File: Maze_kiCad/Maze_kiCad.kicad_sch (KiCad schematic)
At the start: 10 parts, among them J1 Screw_Terminal, U1 ESP32-S3-DevKitC-1, U10 L7805, U2 TCRT5000, U3 TCRT5000, U4 TCRT5000, U5 TCRT5000, U6 TCRT5000, U7 TCRT5000

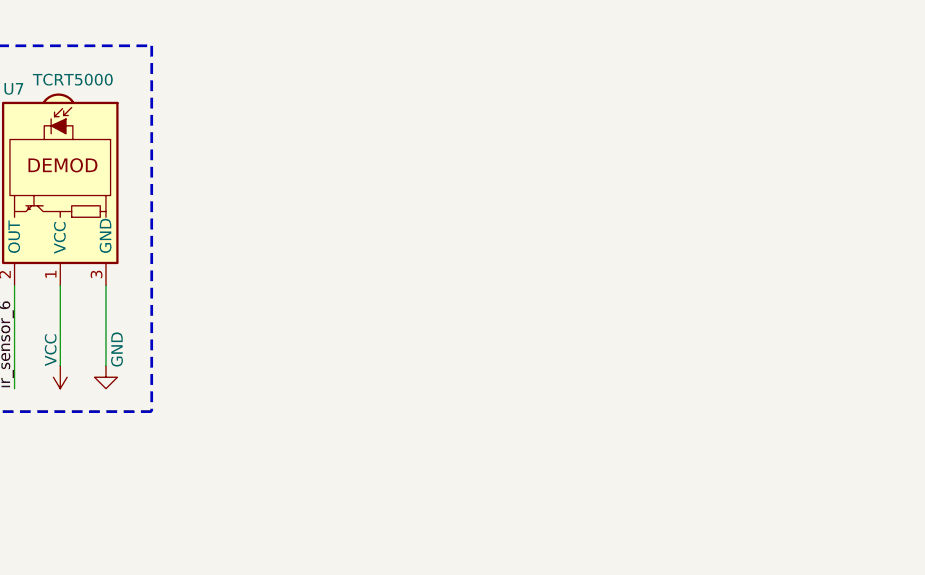
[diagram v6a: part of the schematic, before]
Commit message: Make all connections for drv8835, esp32-s3 and motors inputs
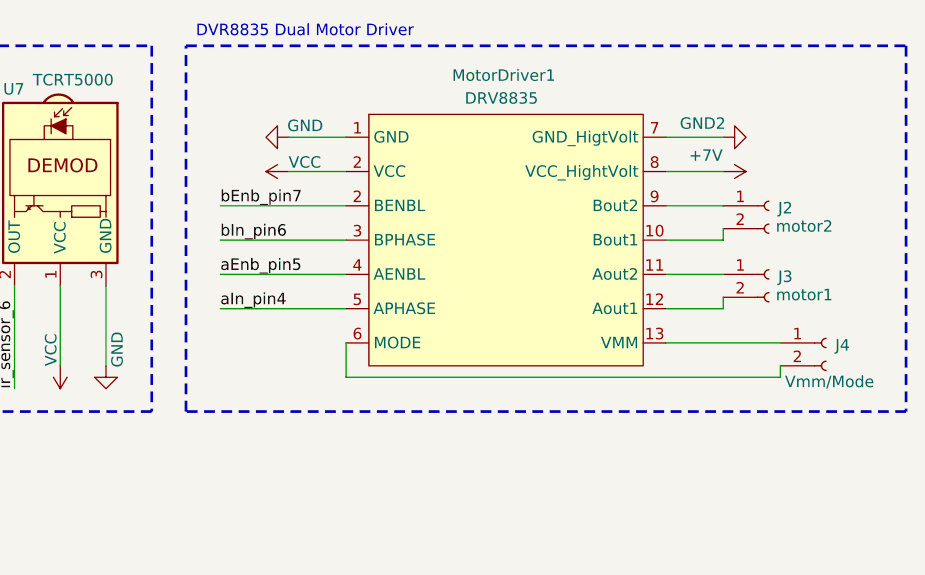
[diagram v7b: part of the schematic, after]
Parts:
- added J2: motor2, Connector_PinSocket_2.54mm:PinSocket_1x02_P2.54mm_Vertical, symbol Connector:Conn_01x02_Socket
- added J3: motor1, Connector_PinSocket_2.54mm:PinSocket_1x02_P2.54mm_Vertical, symbol Connector:Conn_01x02_Socket
- added J4: Vmm/Mode, Connector_PinSocket_2.54mm:PinSocket_1x02_P2.54mm_Vertical, symbol Connector:Conn_01x02_Socket
- added MotorDriver1: DRV8835, drv8835:drv8835, symbol drv8835:DRV8835
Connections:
- net +7V: now also MotorDriver1.8 (VCC_HightVolt)
- net GND: now also MotorDriver1.1 (GND)
- net GND2: now also MotorDriver1.7 (GND_HigtVolt)
- net VCC: now also MotorDriver1.2 (VCC)
- net aEnb_pin5: now also MotorDriver1.4 (AENBL)
- net aIn_pin4: now also MotorDriver1.5 (APHASE)
- net bEnb_pin7: now also MotorDriver1.2 (VCC)
- net bIn_pin6: now also MotorDriver1.3 (BPHASE)
- new net: J4.1 (Pin_1), MotorDriver1.13 (VMM)
- new net: J4.2 (Pin_2), MotorDriver1.6 (MODE)
- new net: J2.1 (Pin_1), MotorDriver1.9 (Bout2)
- new net: J2.2 (Pin_2), MotorDriver1.10 (Bout1)
- new net: J3.1 (Pin_1), MotorDriver1.11 (Aout2)
- new net: J3.2 (Pin_2), MotorDriver1.12 (Aout1)
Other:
- note added: "DVR8835 Dual Motor Driver"

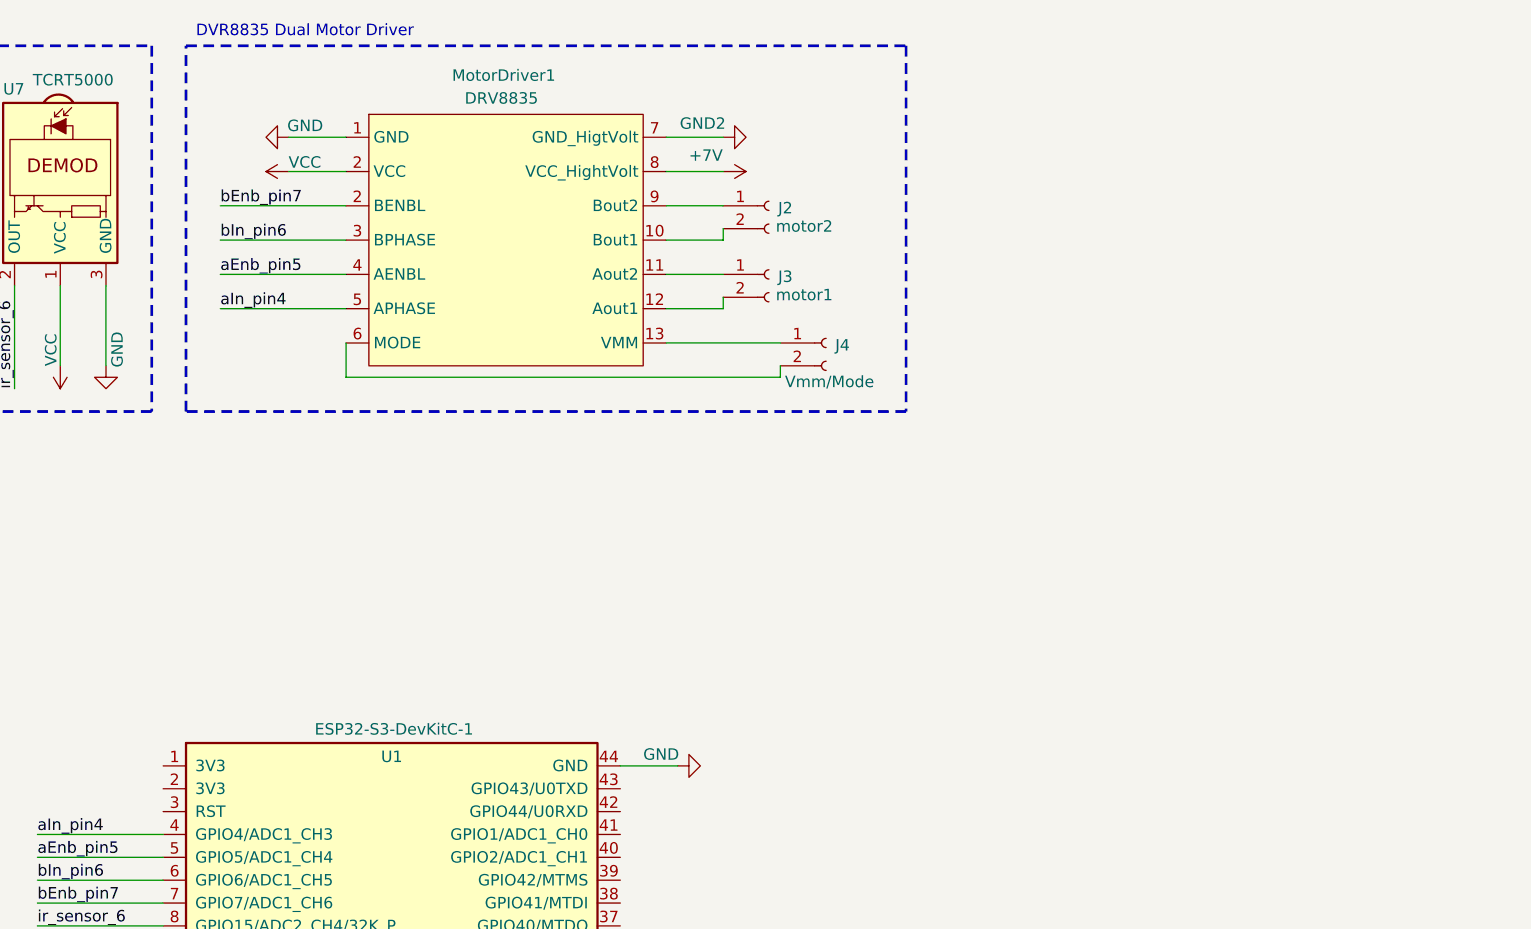
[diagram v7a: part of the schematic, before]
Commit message: Create connections for gyroscope and ultrasonic sensor with esp32-s3
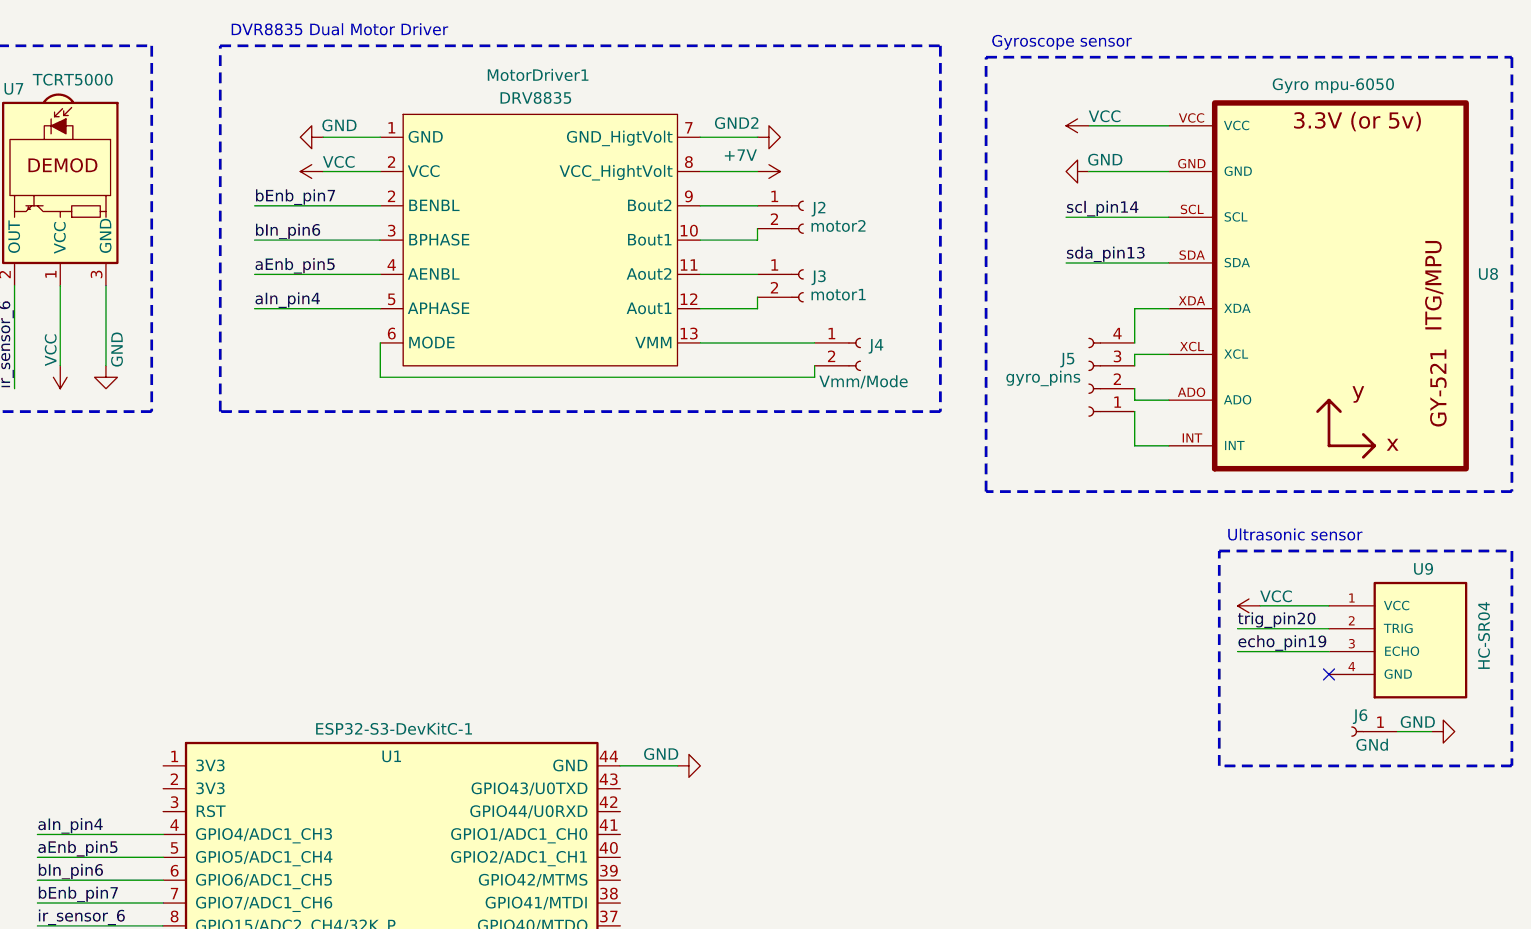
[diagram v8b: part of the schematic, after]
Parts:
- added J5: gyro_pins, symbol Connector:Conn_01x04_Socket
- added J6: GNd, symbol Connector:Conn_01x01_Socket
- added U8: Gyro mpu-6050, mpu6050:GY-521, symbol mpu6050:GY-521
- added U9: HC-SR04, ultrasonic:XCVR_HC-SR04, symbol ultrasonic:HC-SR04
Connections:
- net GND: now also J6.1 (Pin_1), U8.GND
- net VCC: now also U8.VCC, U9.1 (VCC)
- net echo_pin19: now also U9.3 (ECHO)
- net scl_pin14: now also U8.SCL
- net sda_pin13: now also U8.SDA
- net trig_pin20: now also U9.2 (TRIG)
- new net: J5.2 (Pin_2), U8.ADO
- new net: J5.1 (Pin_1), U8.INT
- new net: J5.3 (Pin_3), U8.XCL
- new net: J5.4 (Pin_4), U8.XDA
- no-connect marks 0 -> 1
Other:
- note added: "Gyroscope sensor"
- note added: "Ultrasonic sensor"
- moved on the sheet: J2, J3, J4, MotorDriver1
